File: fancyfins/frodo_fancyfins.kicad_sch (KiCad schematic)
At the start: 102 parts, among them J3 TC2050, U1 AZ1117-5.0, U10 L78L05_SOT89, U11 W25Q128JVP, U12 L78L05_SOT89, U13 L78L05_SOT89, U14 L78L05_SOT89, U15 L78L05_SOT89, U16 L78L05_SOT89, U2 AZ1117-3.3, U3 STM32F103RCTx, U4 MCP2562-E-SN, U5 TPD4E1U06, U6 L78L05_SOT89, U7 L78L05_SOT89, U8 L78L05_SOT89, U9 L78L05_SOT89, Y1 8MHz 12pF

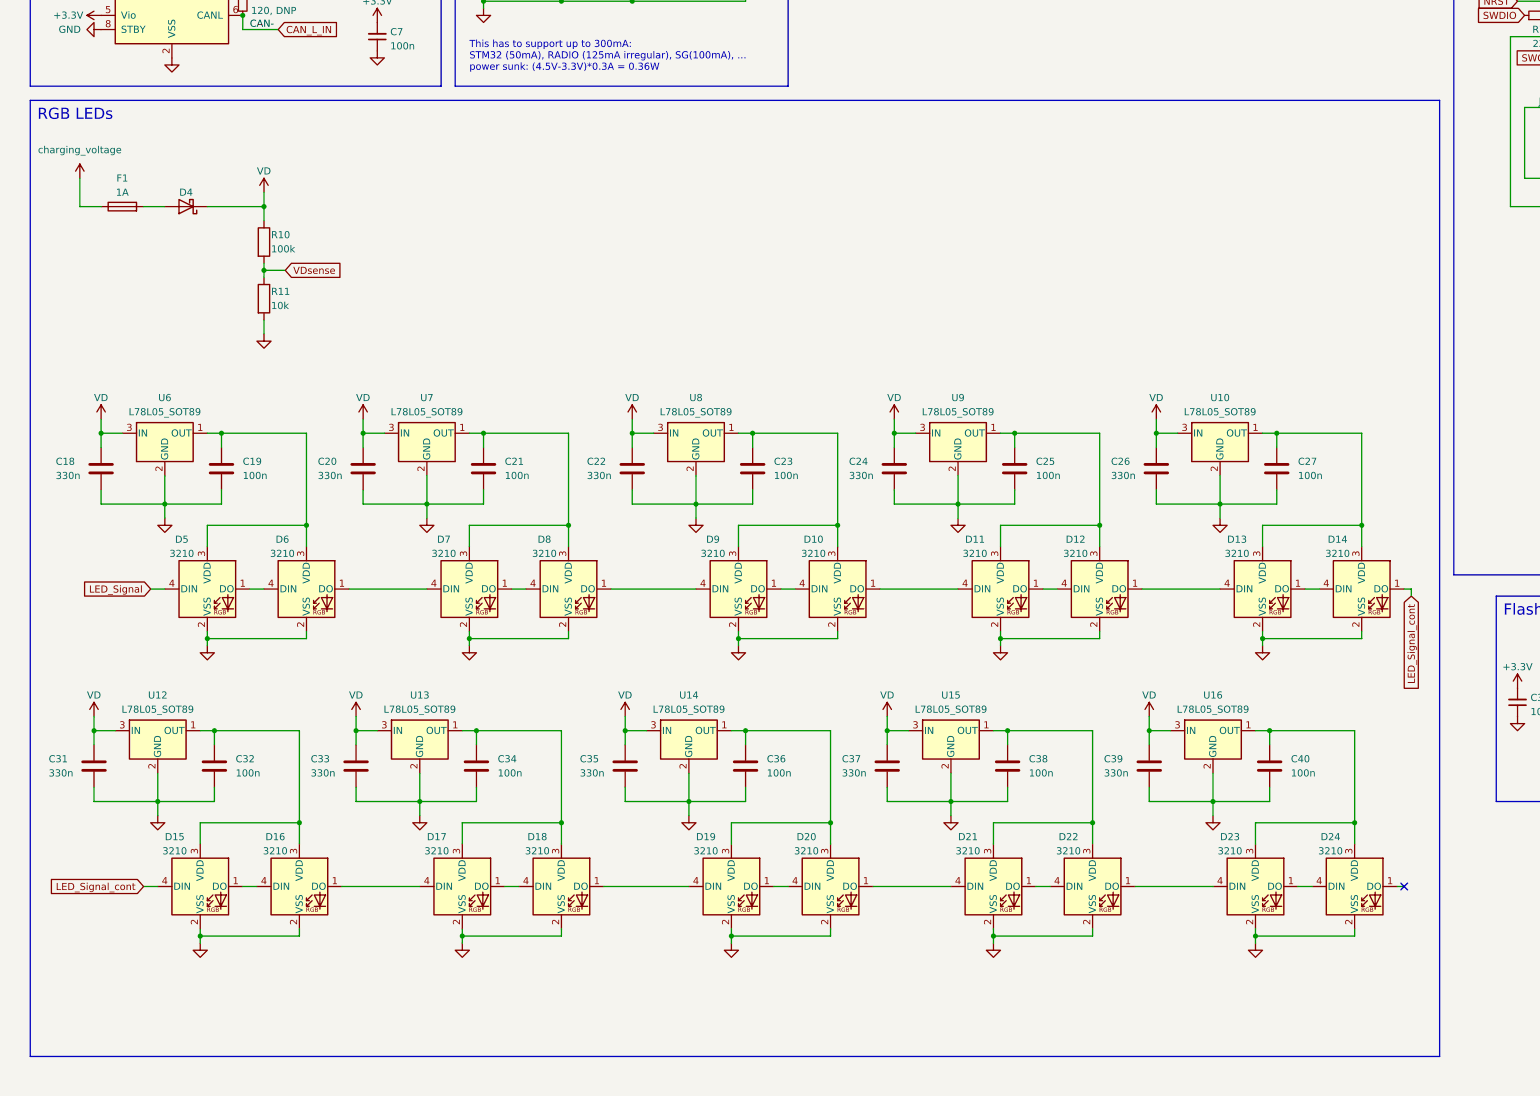
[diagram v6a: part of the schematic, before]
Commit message: changed scematic + examplary layout
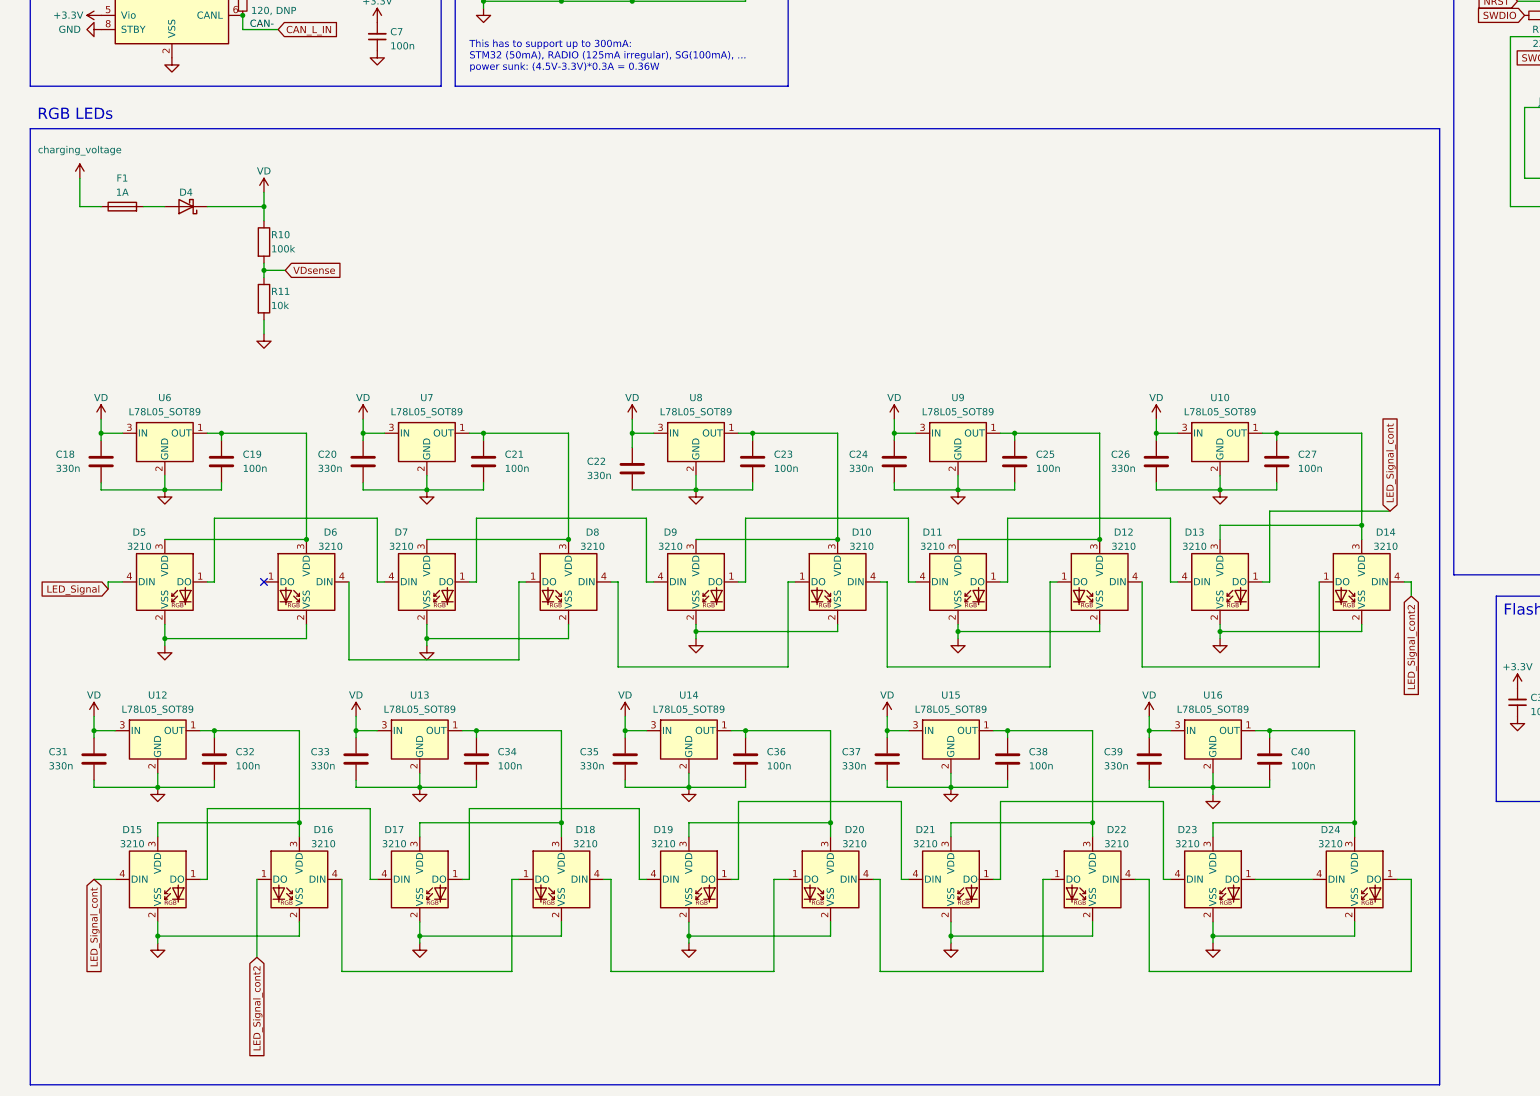
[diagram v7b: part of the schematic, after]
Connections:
- net LED_Signal_cont: now also D13.1 (DO); no longer D14.1 (DO)
- net at D7.1 (DO): now also D9.4 (DIN); no longer D8.4 (DIN)
- net at D7.4 (DIN): now also D5.1 (DO); no longer D6.1 (DO)
- net at D17.1 (DO): now also D19.4 (DIN); no longer D18.4 (DIN)
- net at D17.4 (DIN): now also D15.1 (DO); no longer D16.1 (DO)
- net LED_Signal_cont2: now reaches D14.4 (DIN)
- net LED_Signal_cont2: now also D16.1 (DO); no longer D13.1 (DO)
- net at D13.4 (DIN): now also D11.1 (DO); no longer D12.1 (DO)
- net at D16.4 (DIN): now also D18.1 (DO); no longer D15.1 (DO)
- net at D12.4 (DIN): now also D14.1 (DO); no longer D11.1 (DO)
- net at D6.4 (DIN): now also D8.1 (DO); no longer D5.1 (DO)
- net at D10.4 (DIN): now also D12.1 (DO); no longer D9.1 (DO)
- net at D24.1 (DO): now also D22.4 (DIN)
- net at D19.1 (DO): now also D21.4 (DIN); no longer D20.4 (DIN)
- net at D11.4 (DIN): now also D9.1 (DO); no longer D10.1 (DO)
- net at D21.1 (DO): now also D23.4 (DIN); no longer D22.4 (DIN)
- net at D20.1 (DO): now also D18.4 (DIN); no longer D21.4 (DIN)
- net at D22.1 (DO): now also D20.4 (DIN); no longer D23.4 (DIN)
- new net: D10.1 (DO), D8.4 (DIN)
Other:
- moved on the sheet: C18, C19, C20, C21, C23, C24, C25, C26, C27, C31, C32, C33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

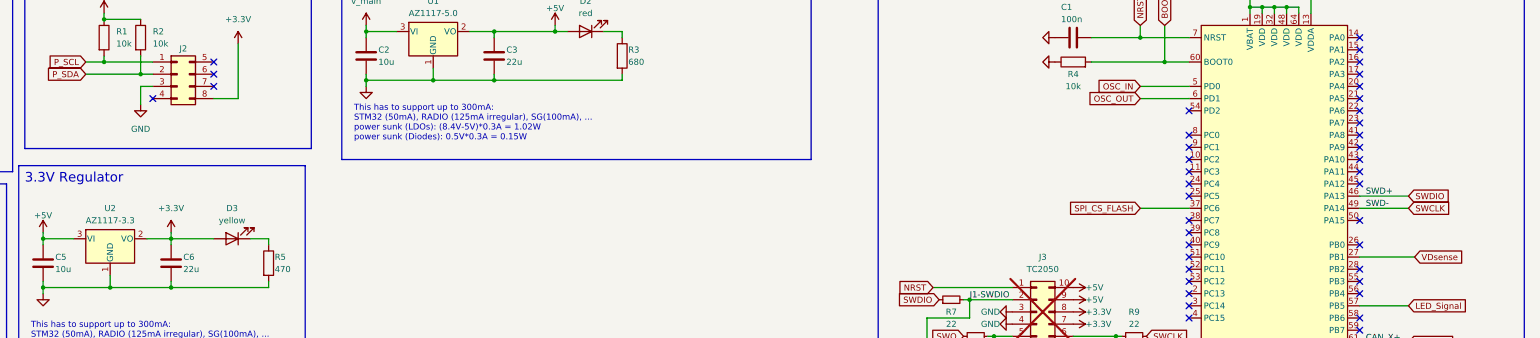
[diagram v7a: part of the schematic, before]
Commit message: began fancyfin routing
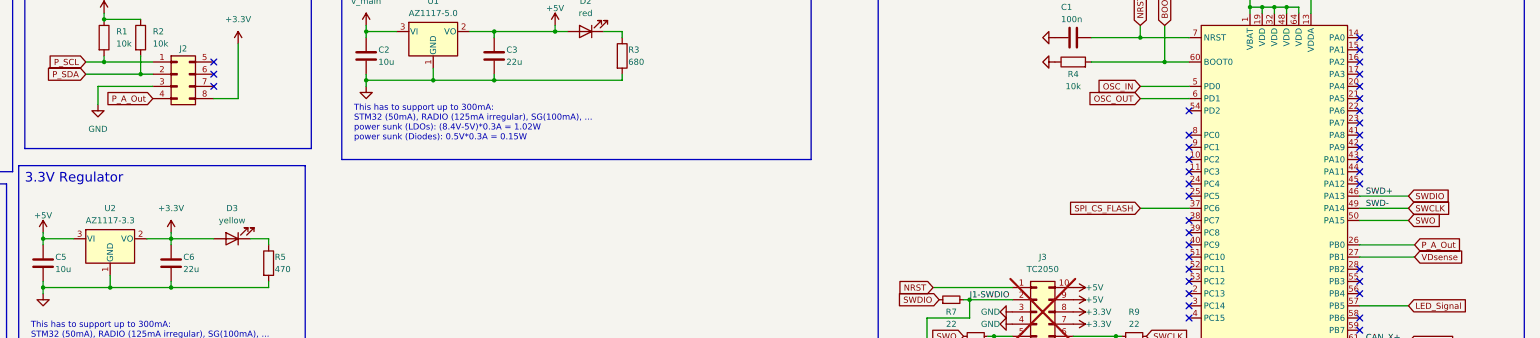
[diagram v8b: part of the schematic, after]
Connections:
- net SWO: now also U3.50 (PA15)
- net P_A_Out: now reaches U3.26 (PB0)
- net P_A_Out: now also J2.4 (Pin_4)
- no-connect marks 44 -> 41
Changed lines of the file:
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@@
 	)
 	(no_connect
-		(at 369.57 74.93)
-	)
-	(no_connect
 		(at 334.01 69.85)
 	)
 	(no_connect
-		(at 118.11 44.45)
-	)
-	(no_connect
 		(at 369.57 36.83)
 	)
@@
 	)
 	(no_connect
-		(at 369.57 69.85)
-	)
-	(no_connect
 		(at 369.57 90.17)
 	)
@@
 	(wire
 		(pts
-			(xy 115.57 41.91) (xy 115.57 45.72)
+			(xy 106.68 41.91) (xy 106.68 45.72)
 		)
 		(stroke
@@
 	(wire
 		(pts
+			(xy 369.57 69.85) (xy 379.73 69.85)
+		)
+		(stroke
+			(width 0)
+			(type default)
+		)
+	)
+	(wire
+		(pts
 			(xy 115.57 39.37) (xy 118.11 39.37)
 		)
@@
 	(wire
 		(pts
+			(xy 369.57 74.93) (xy 381 74.93)
+		)
+		(stroke
+			(width 0)
+			(type default)
+		)
+	)
+	(wire
+		(pts
 			(xy 227.33 168.91) (xy 227.33 171.45)
 		)
@@
 	(wire
 		(pts
-			(xy 115.57 41.91) (xy 118.11 41.91)
+			(xy 106.68 41.91) (xy 118.11 41.91)
 		)
 		(stroke
@@
 		)
 	)
+	(global_label "SWO"
+		(shape input)
+		(at 379.73 69.85 0)
+		(fields_autoplaced yes)
+		(effects
+			(font
+				(size 1.27 1.27)
+			)
+			(justify left)
+		)
+		(property "Intersheetrefs" "${INTERSHEET_REFS}"
+			(at 386.7066 69.85 0)
+			(effects
+				(font
+					(size 1.27 1.27)
+				)
+				(justify left)
+				(hide yes)
+			)
+		)
+	)
 	(global_label "SWCLK"
 		(shape input)
@@
 		)
 	)
+	(global_label "P_A_Out"
+		(shape input)
+		(at 118.11 44.45 180)
+		(fields_autoplaced yes)
+		(effects
+			(font
+				(size 1.27 1.27)
+			)
+			(justify right)
+		)
+		(property "Intersheetrefs" "${INTERSHEET_REFS}"
+			(at 107.6258 44.45 0)
+			(effects
+				(font
+					(size 1.27 1.27)
+				)
+				(justify right)
+				(hide yes)
+			)
+		)
+	)
 	(global_label "VDsense"
 		(shape input)
@@
 		)
 	)
+	(global_label "P_A_Out"
+		(shape input)
+		(at 381 74.93 0)
+		(fields_autoplaced yes)
+		(effects
+			(font
+				(size 1.27 1.27)
+			)
+			(justify left)
+		)
+		(property "Intersheetrefs" "${INTERSHEET_REFS}"
+			(at 391.4842 74.93 0)
+			(effects
+				(font
+					(size 1.27 1.27)
+				)
+				(justify left)
+				(hide yes)
+			)
+		)
+	)
 	(global_label "SPI2_SCK"
 		(shape input)
@@
 		(lib_name "GND_1")
 		(lib_id "power:GND")
-		(at 115.57 45.72 0)
+		(at 106.68 45.72 0)
 		(unit 1)
 		(exclude_from_sim no)
@@
 		(fields_autoplaced yes)
 		(property "Reference" "#PWR013"
-			(at 115.57 52.07 0)
+			(at 106.68 52.07 0)
 			(effects
 				(font
@@
 		)
 		(property "Value" "GND"
-			(at 115.57 50.8 0)
+			(at 106.68 50.8 0)
 			(effects
 				(font
@@
 		)
 		(property "Footprint" ""
-			(at 115.57 45.72 0)
+			(at 106.68 45.72 0)
 			(effects
 				(font
@@
 		)
 		(property "Datasheet" ""
-			(at 115.57 45.72 0)
+			(at 106.68 45.72 0)
 			(effects
 				(font
@@
 		)
 		(property "Description" "Power symbol creates a global label with name \"GND\" , ground"
-			(at 115.57 45.72 0)
+			(at 106.68 45.72 0)
 			(effects
 				(font
